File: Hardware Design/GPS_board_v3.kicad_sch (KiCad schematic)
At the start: 15 parts, among them IC2 SN65HVD231QDR, U1 STM32F042F4Px, U5 MAX-M8W

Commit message: final updated board + prod files
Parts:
- removed J1: ~, Connector_PinHeader_2.54mm:PinHeader_1x02_P2.54mm_Vertical, symbol Connector:Samtec_ASP-134486-01
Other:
- note removed: "MAX-M8 I2C Config"
- moved on the sheet: J4A
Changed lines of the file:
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@@
 	(wire
 		(pts
-			(xy 95.25 185.42) (xy 95.25 186.69)
+			(xy 127 148.59) (xy 127 149.86)
 		)
 		(stroke
@@
 		)
 	)
+	(polyline
+		(pts
+			(xy 12.7 109.22) (xy 96.52 109.22)
+		)
+		(stroke
+			(width 0)
+			(type default)
+		)
+	)
+	(polyline
+		(pts
+			(xy 185.42 12.7) (xy 185.42 170.18)
+		)
+		(stroke
+			(width 0)
+			(type default)
+		)
+	)
 	(wire
 		(pts
-			(xy 95.25 186.69) (xy 110.49 186.69)
+			(xy 127 149.86) (xy 142.24 149.86)
 		)
 		(stroke
@@
 		)
 	)
+	(polyline
+		(pts
+			(xy 96.52 12.7) (xy 96.52 203.2)
+		)
+		(stroke
+			(width 0)
+			(type default)
+		)
+	)
 	(wire
 		(pts
@@
 		)
 	)
+	(polyline
+		(pts
+			(xy 96.52 109.22) (xy 266.7 109.22)
+		)
+		(stroke
+			(width 0)
+			(type default)
+		)
+	)
 	(text "MAX-M8W GNSS Module"
 		(exclude_from_sim no)
@@
 		)
 	)
-	(text "MAX-M8 I2C Config"
-		(exclude_from_sim no)
-		(at 121.92 138.0744 0)
-		(effects
-			(font
-				(face "KiCad Font")
-				(size 2.8956 2.8956)
-			)
-			(justify left top)
-		)
-	)
 	(text "STM SWD"
 		(exclude_from_sim no)
-		(at 99.568 174.752 0)
+		(at 131.318 137.922 0)
 		(effects
 			(font
@@
 	(global_label "SWCLK"
 		(shape input)
-		(at 110.49 189.23 180)
+		(at 142.24 152.4 180)
 		(fields_autoplaced yes)
 		(effects
@@
 		)
 		(property "Intersheetrefs" "${INTERSHEET_REFS}"
-			(at 101.2758 189.23 0)
+			(at 133.0258 152.4 0)
 			(effects
 				(font
@@
 		)
 	)
-	(global_label "SCL"
-		(shape input)
-		(at 143.51 156.21 180)
-		(effects
-			(font
-				(size 1.27 1.27)
-			)
-			(justify right)
-		)
-		(property "Intersheetrefs" "${INTERSHEET_REFS}"
-			(at 143.51 156.21 0)
-			(effects
-				(font
-					(size 1.27 1.27)
-				)
-				(hide yes)
-			)
-		)
-	)
 	(global_label "CAN_RX"
 		(shape output)
@@
 		)
 	)
-	(global_label "SDA"
-		(shape bidirectional)
-		(at 143.51 158.75 180)
-		(effects
-			(font
-				(size 1.27 1.27)
-			)
-			(justify right)
-		)
-		(property "Intersheetrefs" "${INTERSHEET_REFS}"
-			(at 143.51 158.75 0)
-			(effects
-				(font
-					(size 1.27 1.27)
-				)
-				(hide yes)
-			)
-		)
-	)
 	(global_label "SCL"
 		(shape input)
@@
 	(global_label "STM_RST"
 		(shape input)
-		(at 110.49 184.15 180)
+		(at 142.24 147.32 180)
 		(fields_autoplaced yes)
 		(effects
@@
 		)
 		(property "Intersheetrefs" "${INTERSHEET_REFS}"
-			(at 99.4616 184.15 0)
+			(at 131.2116 147.32 0)
 			(effects
 				(font
@@
 	(global_label "SWDIO"
 		(shape bidirectional)
-		(at 110.49 194.31 180)
+		(at 142.24 157.48 180)
 		(fields_autoplaced yes)
 		(effects
@@
 		)
 		(property "Intersheetrefs" "${INTERSHEET_REFS}"
-			(at 100.5273 194.31 0)
+			(at 132.2773 157.48 0)
 			(effects
 				(font
@@
 	(symbol
 		(lib_id "power:GND")
-		(at 110.49 191.77 270)
+		(at 142.24 154.94 270)
 		(unit 1)
 		(exclude_from_sim no)
@@
 		(dnp no)
 		(property "Reference" "#PWR018"
-			(at 104.14 191.77 0)
+			(at 135.89 154.94 0)
 			(effects
 				(font
@@
 		)
 		(property "Value" "GND"
-			(at 105.664 191.77 90)
+			(at 137.414 154.94 90)
 			(effects
 				(font
@@
 		)
 		(property "Footprint" ""
-			(at 110.49 191.77 0)
+			(at 142.24 154.94 0)
 			(effects
 				(font
@@
 		)
 		(property "Datasheet" ""
-			(at 110.49 191.77 0)
+			(at 142.24 154.94 0)
 			(effects
 				(font
@@
 		)
 		(property "Description" "Power symbol creates a global label with name \"GND\" , ground"
-			(at 110.49 191.77 0)
+			(at 142.24 154.94 0)
 			(effects
 				(font
@@
 	(symbol
 		(lib_id "power:+3V3")
-		(at 95.25 185.42 0)
+		(at 127 148.59 0)
 		(unit 1)
 		(exclude_from_sim no)
@@
 		(dnp no)
 		(property "Reference" "#PWR019"
-			(at 95.25 189.23 0)
+			(at 127 152.4 0)
 			(effects
 				(font
@@
 		)
 		(property "Value" "+3V3"
-			(at 94.742 181.102 0)
+			(at 126.492 144.272 0)
 			(effects
 				(font
@@
 		)
 		(property "Footprint" ""
-			(at 95.25 185.42 0)
+			(at 127 148.59 0)
 			(effects
 				(font
@@
 		)
 		(property "Datasheet" ""
-			(at 95.25 185.42 0)
+			(at 127 148.59 0)
 			(effects
 				(font
@@
 		)
 		(property "Description" "Power symbol creates a global label with name \"+3V3\""
-			(at 95.25 185.42 0)
+			(at 127 148.59 0)
 			(effects
 				(font
@@
 		(lib_name "Samtec_ASP-134486-01_2")
 		(lib_id "Connector:Samtec_ASP-134486-01")
-		(at 113.03 177.8 0)
+		(at 144.78 140.97 0)
 		(unit 1)
 		(exclude_from_sim no)
@@
 		(fields_autoplaced yes)
 		(property "Reference" "J4"
-			(at 111.252 180.848 0)
+			(at 143.002 144.018 0)
 			(effects
 				(font
@@
 		)
 		(property "Value" "~"
-			(at 100.838 180.848 0)
+			(at 132.588 144.018 0)
 			(effects
 				(font
@@
 		)
 		(property "Footprint" "Connector_PinHeader_2.54mm:PinHeader_1x05_P2.54mm_Vertical"
-			(at 114.3 123.19 0)
+			(at 146.05 86.36 0)
 			(effects
 				(font
@@
 		)
 		(property "Datasheet" "http://suddendocs.samtec.com/prints/asp-134486-01-mkt.pdf"
-			(at 116.84 124.46 0)
+			(at 148.59 87.63 0)
 			(effects
 				(font
@@
 		)
 		(property "Description" "Connector array, 10x40, 1.27mm pitch, carrier-card, receptacle, gold finish, VITA 57.1 FMC, SMD"
-			(at 113.03 177.8 0)
+			(at 144.78 140.97 0)
 			(effects
 				(font
@@
 					(unit 1)
 				)
-			)
-		)
-	)
-	(symbol
-		(lib_id "Connector:Samtec_ASP-134486-01")
-		(at 146.05 149.86 0)
-		(unit 1)
-		(exclude_from_sim no)
-		(in_bom yes)
-		(on_board yes)
-		(dnp no)
-		(fields_autoplaced yes)
-		(property "Reference" "J1"
-			(at 144.272 152.908 0)
-			(effects
-				(font
-					(size 1.27 1.27)
-				)
-				(justify left)
-			)
-		)
-		(property "Value" "~"
-			(at 133.858 152.908 0)
-			(effects
-				(font
-					(size 1.27 1.27)
-				)
-				(justify left)
-			)
-		)
-		(property "Footprint" "Connector_PinHeader_2.54mm:PinHeader_1x02_P2.54mm_Vertical"
-			(at 147.32 95.25 0)
-			(effects
-				(font
-					(size 1.27 1.27)
-				)
-				(hide yes)
-			)
-		)
-		(property "Datasheet" "http://suddendocs.samtec.com/prints/asp-134486-01-mkt.pdf"
-			(at 149.86 96.52 0)
-			(effects
-				(font
-					(size 1.27 1.27)
-				)
-				(hide yes)
-			)
-		)
-		(property "Description" "Connector array, 10x40, 1.27mm pitch, carrier-card, receptacle, gold finish, VITA 57.1 FMC, SMD"
-			(at 146.05 149.86 0)
-			(effects
-				(font
-					(size 1.27 1.27)
-				)
-				(hide yes)
-			)
-		)
-		(pin "H2"
-		)
-		(pin "J1"
-		)
-		(pin "J2"
-		)
-		(pin "K1"
-		)
-		(pin "K2"
-		)
-		(pin "C1"
-		)
-		(pin "E2"
-		)
-		(pin "G2"
-		)
-		(pin "E1"
-		)
-		(pin "F2"
-		)
-		(pin "D1"
-		)
-		(pin "B1"
-		)
-		(pin "B2"
-		)
-		(pin "D2"
-		)
-		(pin "1"
-		)
-		(pin "F1"
-		)
-		(pin "H1"
-		)
-		(pin "2"
-		)
-		(pin "C2"
-		)
-		(pin "G1"
-		)
-		(instances
-			(project "GPS_board_v3"
-				(path "/c3e0ad51-8a79-42ff-b905-b5467e5e45fa"
-					(reference "J1")
-					(unit 1)
-				)

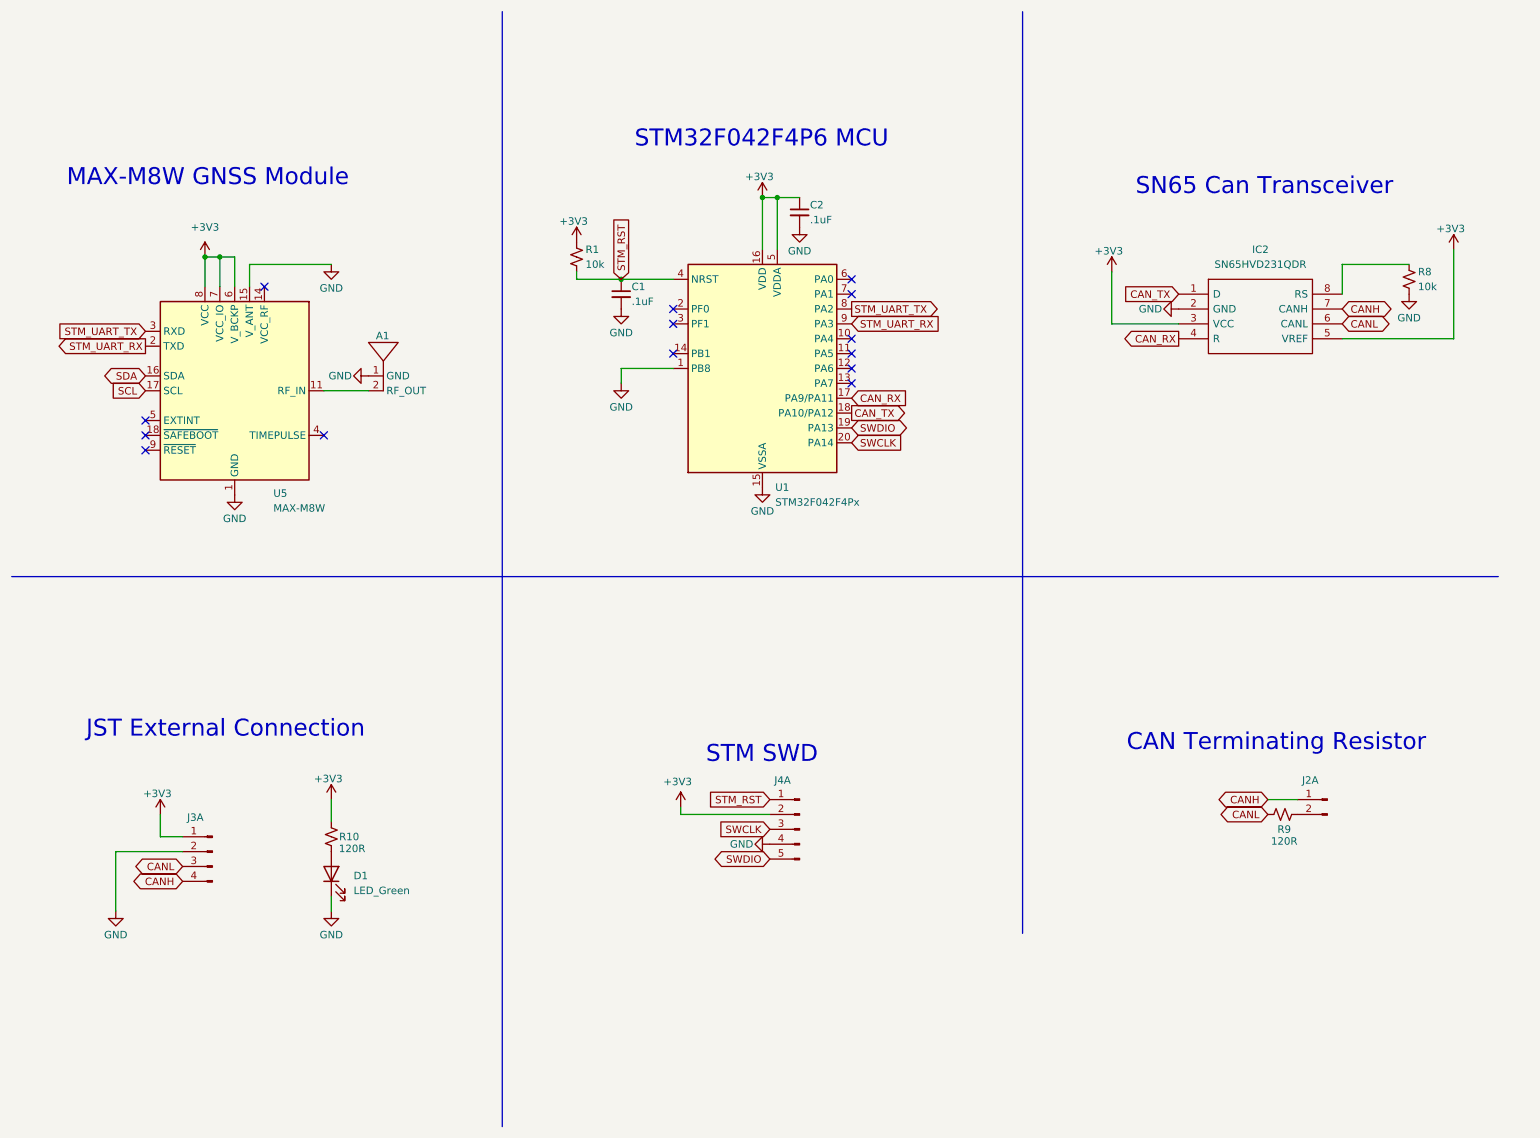
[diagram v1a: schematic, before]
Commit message: Added testing headers.
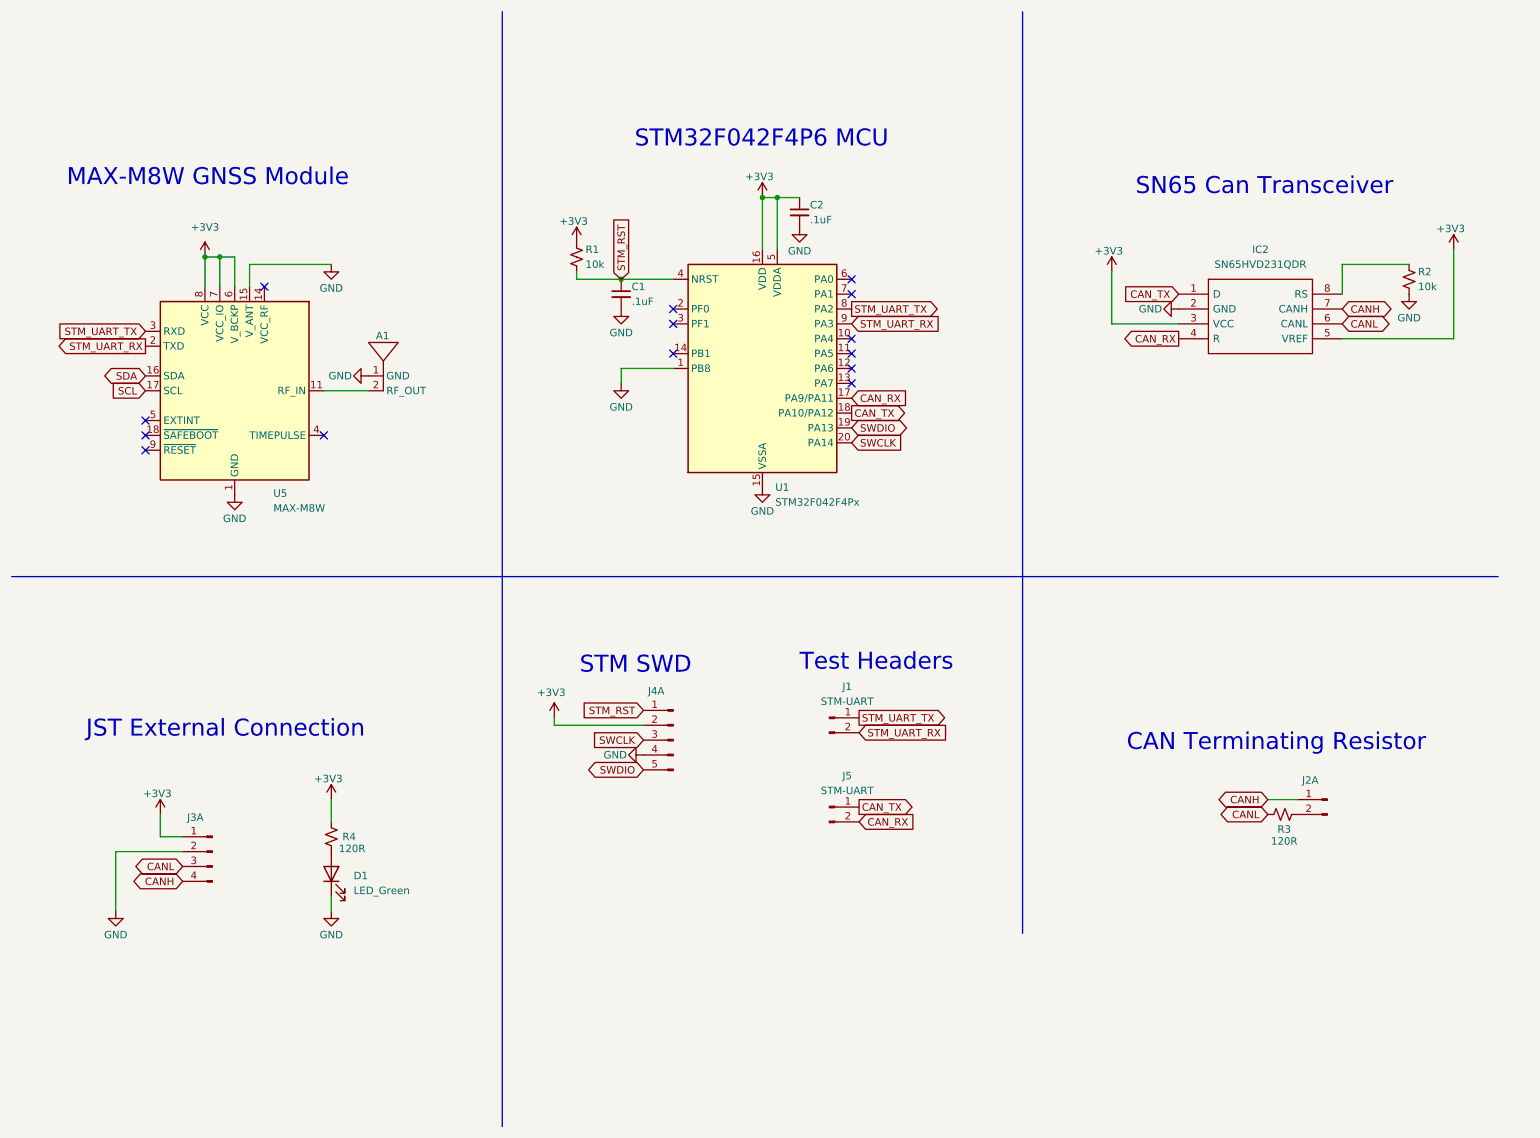
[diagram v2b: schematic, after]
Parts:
- added J1, J5: STM-UART, Connector_PinHeader_2.54mm:PinHeader_1x02_P2.54mm_Vertical, symbol Connector:Conn_01x02_Pin
- A1, J2, J3, J4: value ~ -> (none)
- renumbered R8 to R2, R9 to R3, R10 to R4
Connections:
- net CAN_RX: now also J5.2 (Pin_2)
- net CAN_TX: now also J5.1 (Pin_1)
- net STM_UART_RX: now also J1.2 (Pin_2)
- net STM_UART_TX: now also J1.1 (Pin_1)
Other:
- note added: "Test Headers"
- moved on the sheet: J4A
